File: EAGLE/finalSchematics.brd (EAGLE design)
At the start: 100 x 80 mm, 13 parts, among them IC1 STM32F103RBT, P1 DM3CS-SF, Q1 8MHz 131-220

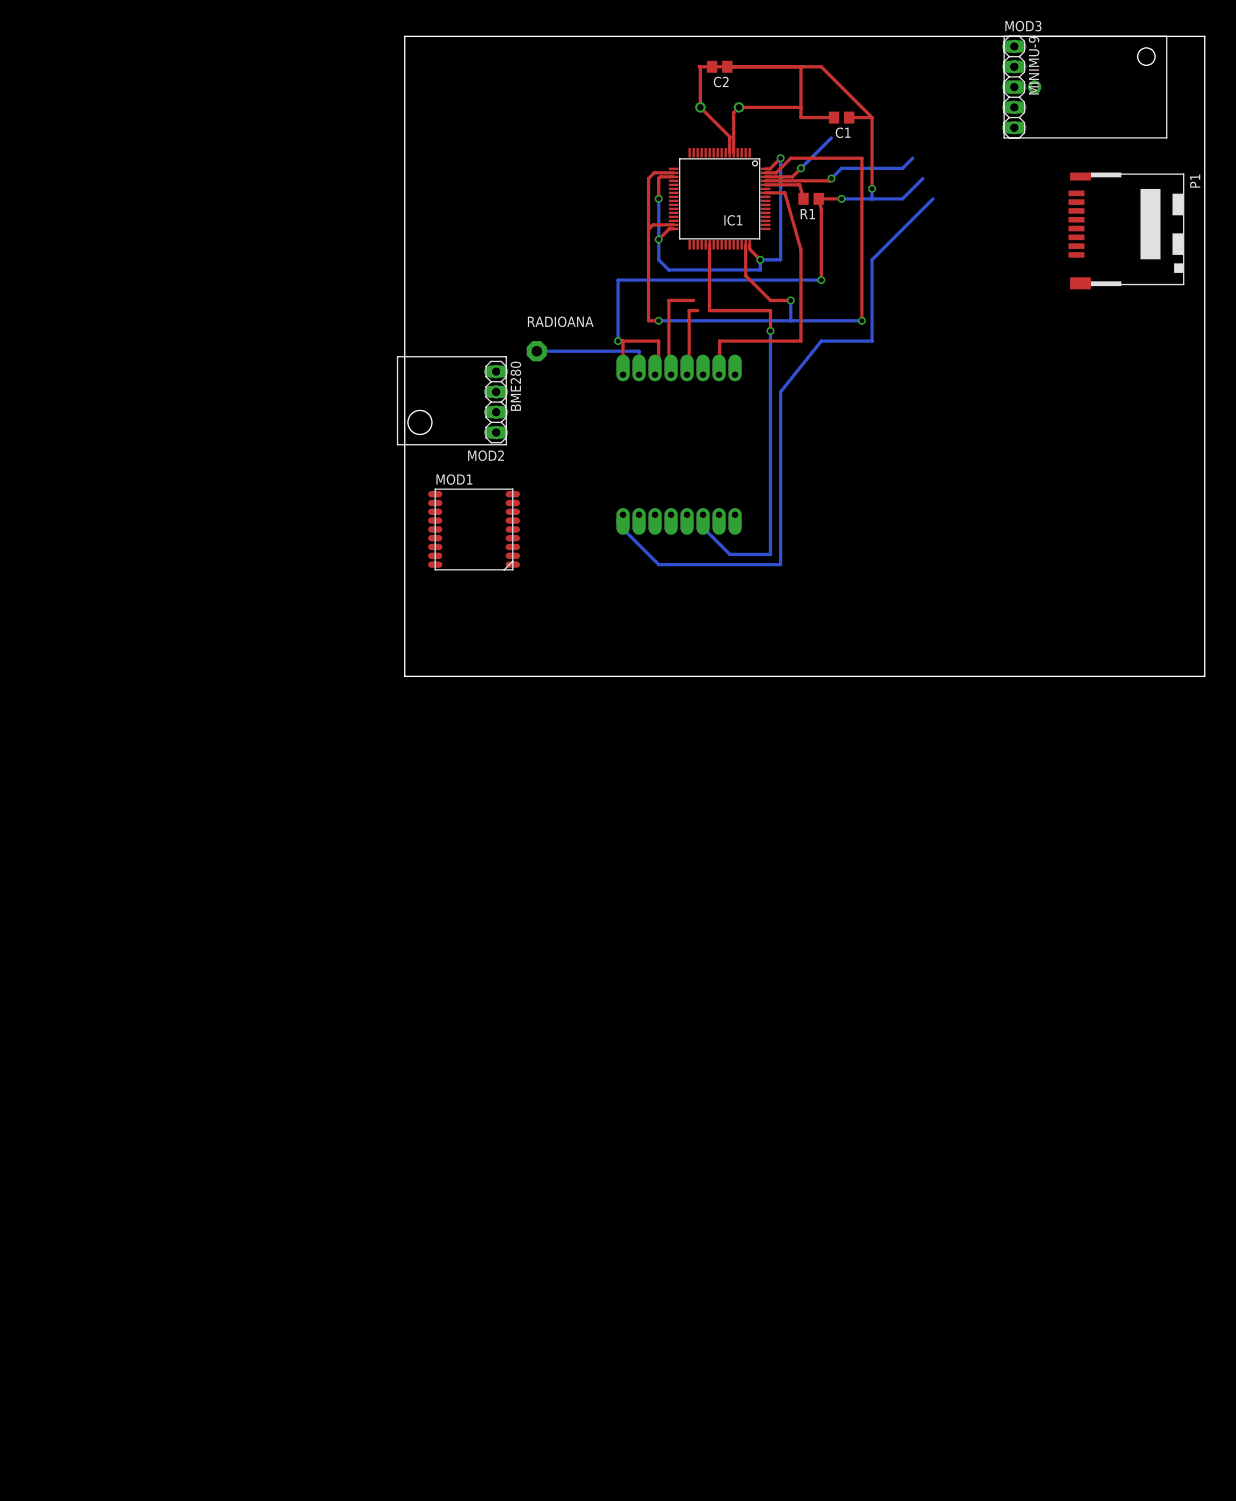
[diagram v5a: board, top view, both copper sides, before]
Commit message: Add SD package, fix powers supply of MCU
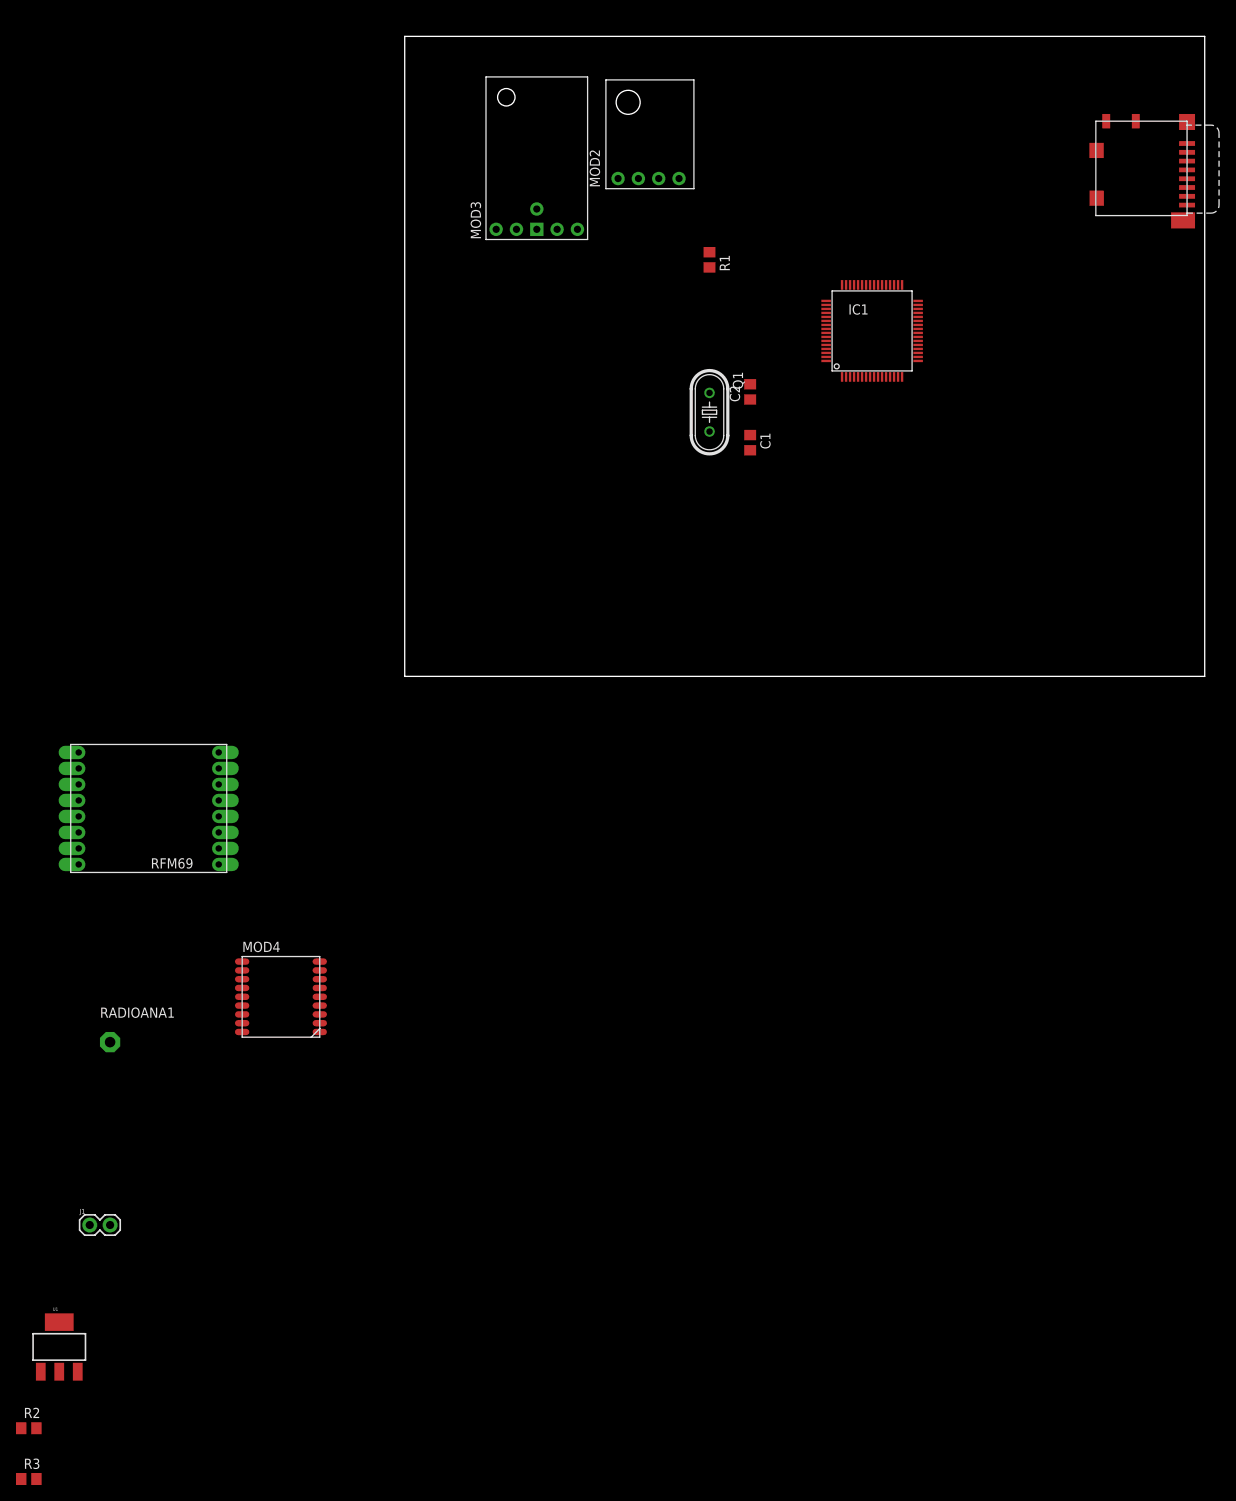
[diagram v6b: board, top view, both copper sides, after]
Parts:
- removed BME280: (no value), pinhead:1X04
- removed MINIMU-9: (no value), pinhead:1X05
- removed MOD1: GPS, components:L70B-GPS
- removed P1: DM3CS-SF, DM3CS-SF:HRS_DM3CS-SF
- removed RADIOANA: (no value), discrete:PAD-01
- removed U$1: RFM69, RFM69mod:20X16BOARD
- added J1: (no value), SparkFun-Connectors:1X02
- added MOD4: GPS, components:L70B-GPS
- added R2, R3: 10k 901-655, rcl:R0805
- added RADIOANA1: (no value), discrete:PAD-01
- added SD1: (no value), components:MOLEX-SD-104031
- added U$2: RFM69, RFM69mod:20X16BOARD
- added U1: LM1117-3.3, SparkFun-IC-Power:SOT223
- IC1: device micro-stm_v3:LQFP64 -> components:LQFP64
- MOD2: value (none) -> BME280
- moved MOD3 62.3 mm to (16.5, 55.9), turned to 90 degrees
- moved C1 42.2 mm to (43.2, 29.2), turned to 270 degrees
- moved C2 40.8 mm to (43.2, 35.6), turned to 90 degrees
- moved Q1 38.1 mm to (38.1, 33.0), flipped to the top, turned to 270 degrees
- moved MOD2 31.4 mm to (35.6, 61.0), turned to 90 degrees
- moved IC1 25.2 mm to (58.4, 43.2), turned to 0 degrees
- moved R1 14.8 mm to (38.1, 52.1), turned to 270 degrees
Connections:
- removed net CS: IC1.43, P1.2
- removed net MISO: IC1.35, P1.7
- removed net MOSI: IC1.36, P1.3
- removed net SCK: IC1.34, P1.5
- removed net VDDA: IC1.13
- removed net VSS: IC1.18, IC1.31, IC1.47, IC1.63
- removed net VSSA: IC1.12
- new net N$5: RADIOANA1.1, U$2.ANA
- net +3V3: now also IC1.13, IC1.19, IC1.32, IC1.48, IC1.64, MOD2.VIN, MOD3.VDD, R2.2, R3.2, SD1.VDD, U$2.3.3V, U1.2, U1.4; no longer BME280.1, MINIMU-9.5, P1.4, U$1.3.3V
- net DIO1_MODEM: now also U$2.DIO1; no longer IC1.38, U$1.DIO1
- net GND: now also IC1.12, IC1.18, IC1.31, IC1.47, IC1.63, J1.2, MOD2.GND, MOD3.GND, MOD4.GND1, MOD4.GND2, MOD4.GND3, SD1.GND@1, SD1.GND@2, SD1.GND@3, SD1.GND@4, SD1.SW1, SD1.SW2, SD1.VSS, U$2.GND@1, U$2.GND@2, U1.1; no longer BME280.2, MINIMU-9.3, MOD1.GND1, MOD1.GND2, MOD1.GND3, P1.6, U$1.GND@1, U$1.GND@2
- net MISO_MODEM: now also U$2.MISO; no longer U$1.MISO
- net MOSI_MODEM: now also U$2.MOSI; no longer U$1.MOSI
- net N$3: now also J1.1, U1.3; no longer RADIOANA.1, U$1.ANA
- net NC: now also U$2.NC; no longer U$1.NC
- net NSS_MODEM: now also U$2.NSS; no longer IC1.58, U$1.NSS
- net RX: now also MOD4.RXD1; no longer MOD1.RXD1
- net SCK_MODEM: now also U$2.SCK; no longer U$1.SCK
- net SCL: now also MOD2.SCL, MOD3.SCL, R3.1; no longer BME280.3, IC1.19, IC1.32, IC1.48, IC1.64, MINIMU-9.1
- net SDA: now also MOD2.SDA, MOD3.SDA, R2.1; no longer BME280.4, MINIMU-9.2
- net TX: now also MOD4.TXD1; no longer MOD1.TXD1
- net VCC: now also MOD4.VCC; no longer MOD1.VCC
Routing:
- net GND: track 105.6 -> 0.00 mm, vias 4 -> 0
- net VSS: track 97.7 -> 0.00 mm, vias 3 -> 0
- net +3V3: track 80.8 -> 0.00 mm
- net SCL: track 68.7 -> 0.00 mm, vias 5 -> 0
- net DIO1_MODEM: track 58.2 -> 0.00 mm, vias 1 -> 0
- net NSS_MODEM: track 35.6 -> 0.00 mm
- net N$1: track 30.2 -> 0.00 mm
- net N$2: track 19.2 -> 0.00 mm
- net N$3: track 15.7 -> 0.00 mm
- net SCK_MODEM: track 12.6 -> 0.00 mm
- net SDA: track 10.2 -> 0.00 mm, vias 1 -> 0
- net MISO_MODEM: track 9.34 -> 0.00 mm
- net BOOT0: track 6.06 -> 0.00 mm

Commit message: Connect modules
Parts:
- moved U$2 64.3 mm to (24.1, 15.2)
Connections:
- removed net DIO1_MODEM: U$2.DIO1
- removed net MISO_MODEM: U$2.MISO
- removed net MOSI_MODEM: U$2.MOSI
- removed net NSS_MODEM: U$2.NSS
- removed net SCK_MODEM: U$2.SCK
- removed net VCC: MOD4.VCC
- new net CS-RAD: IC1.41, U$2.NSS
- new net CS-SD: IC1.20, SD1.CD/DAT3
- new net DIO0: IC1.44, U$2.DIO0
- new net MISO: IC1.22, SD1.DAT0, U$2.MISO
- new net MOSI: IC1.23, SD1.CMD, U$2.MOSI
- new net N$6: MOD4.RF_IN
- new net SCK: IC1.21, SD1.CLK, U$2.SCK
- net +3V3: now also MOD4.VCC
- net RX: now also IC1.42
- net TX: now also IC1.43
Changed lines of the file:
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@@
 <?xml version="1.0" encoding="utf-8"?>
 <!DOCTYPE eagle SYSTEM "eagle.dtd">
-<eagle version="8.1.0">
+<eagle version="8.0.0">
 <drawing>
 <settings>
@@
 <element name="R1" library="rcl" package="R0805" value="10k 901-655" x="38.1" y="52.07" rot="R270"/>
 <element name="SD1" library="components" package="MOLEX-SD-104031" value="" x="97.79" y="63.5" rot="R90"/>
-<element name="U$2" library="RFM69mod" package="20X16BOARD" value="RFM69" x="-31.75" y="-16.51"/>
+<element name="U$2" library="RFM69mod" package="20X16BOARD" value="RFM69" x="24.13" y="15.24"/>
 <element name="RADIOANA1" library="discrete" package="PAD-01" value="" x="-36.83" y="-45.72"/>
 <element name="MOD4" library="components" package="L70B-GPS" value="GPS" x="-20.32" y="-44.45"/>
@@
 <wire x1="29.21" y1="62.23" x2="38.1" y2="53.02" width="0" layer="19" extent="1-1"/>
 <wire x1="16.51" y1="55.88" x2="29.21" y2="62.23" width="0" layer="19" extent="1-1"/>
-<wire x1="-23.25" y1="-19.51" x2="43.18" y2="30.16" width="0" layer="19" extent="1-1"/>
-<wire x1="-23.25" y1="-23.51" x2="-23.25" y2="-19.51" width="0" layer="19" extent="1-1"/>
-<wire x1="-20.32" y1="-35.65" x2="-23.25" y2="-23.51" width="0" layer="19" extent="1-1"/>
+<wire x1="32.63" y1="12.24" x2="43.18" y2="30.16" width="0" layer="19" extent="1-1"/>
+<wire x1="32.63" y1="8.24" x2="32.63" y2="12.24" width="0" layer="19" extent="1-1"/>
+<wire x1="-20.32" y1="-35.65" x2="32.63" y2="8.24" width="0" layer="19" extent="1-1"/>
 <wire x1="-20.32" y1="-37.85" x2="-20.32" y2="-35.65" width="0" layer="19" extent="1-1"/>
 <wire x1="-10.62" y1="-44.45" x2="-20.32" y2="-37.85" width="0" layer="19" extent="1-1"/>
@@
 <signal name="NC">
 <contactref element="U$2" pad="NC"/>
-</signal>
-<signal name="VCC">
-<contactref element="MOD4" pad="VCC"/>
 </signal>
 <signal name="VBAT">
@@
 <contactref element="R2" pad="2"/>
 <contactref element="R3" pad="2"/>
+<contactref element="MOD4" pad="VCC"/>
 <wire x1="64.17" y1="46.93" x2="97.79" y2="63.305" width="0" layer="19" extent="1-1"/>
 <wire x1="64.17" y1="40.43" x2="64.17" y2="46.93" width="0" layer="19" extent="1-1"/>
@@
 <wire x1="26.67" y1="62.23" x2="54.67" y2="48.93" width="0" layer="19" extent="1-1"/>
 <wire x1="21.59" y1="55.88" x2="26.67" y2="62.23" width="0" layer="19" extent="1-1"/>
-<wire x1="-40.75" y1="-23.51" x2="21.59" y2="55.88" width="0" layer="19" extent="1-1"/>
-<wire x1="-43.18" y1="-80.721" x2="-40.75" y2="-23.51" width="0" layer="19" extent="1-1"/>
+<wire x1="-10.62" y1="-36.75" x2="21.59" y2="55.88" width="0" layer="19" extent="1-1"/>
+<wire x1="15.13" y1="8.24" x2="-10.62" y2="-36.75" width="0" layer="19" extent="1-1"/>
+<wire x1="-43.18" y1="-80.721" x2="-10.62" y2="-36.75" width="0" layer="19" extent="1-1"/>
 <wire x1="-43.18" y1="-86.9188" x2="-43.18" y2="-80.721" width="0" layer="19" extent="1-1"/>
 <wire x1="-46.04" y1="-93.98" x2="-43.18" y2="-86.9188" width="0" layer="19" extent="1-1"/>
@@
 <wire x1="38.1" y1="30.607" x2="43.18" y2="28.26" width="0" layer="19" extent="1-1"/>
 </signal>
-<signal name="MOSI_MODEM">
-<contactref element="U$2" pad="MOSI"/>
-</signal>
-<signal name="SCK_MODEM">
-<contactref element="U$2" pad="SCK"/>
-</signal>
-<signal name="DIO1_MODEM">
-<contactref element="U$2" pad="DIO1"/>
-</signal>
-<signal name="NSS_MODEM">
+<signal name="CS-RAD">
 <contactref element="U$2" pad="NSS"/>
-</signal>
-<signal name="MISO_MODEM">
-<contactref element="U$2" pad="MISO"/>
+<contactref element="IC1" pad="41"/>
+<wire x1="32.63" y1="20.24" x2="58.17" y2="48.93" width="0" layer="19" extent="1-1"/>
 </signal>
 <signal name="RX">
 <contactref element="MOD4" pad="RXD1"/>
+<contactref element="IC1" pad="42"/>
+<wire x1="-10.62" y1="-42.25" x2="57.67" y2="48.93" width="0" layer="19" extent="1-1"/>
 </signal>
 <signal name="TX">
 <contactref element="MOD4" pad="TXD1"/>
+<contactref element="IC1" pad="43"/>
+<wire x1="-10.62" y1="-43.35" x2="57.17" y2="48.93" width="0" layer="19" extent="1-1"/>
 </signal>
 <signal name="N$5">
 <contactref element="U$2" pad="ANA"/>
 <contactref element="RADIOANA1" pad="1"/>
-<wire x1="-23.25" y1="-21.51" x2="-36.83" y2="-45.72" width="0" layer="19" extent="1-1"/>
+<wire x1="32.63" y1="10.24" x2="-36.83" y2="-45.72" width="0" layer="19" extent="1-1"/>
 </signal>
 <signal name="N$3">
@@
 <wire x1="-39.37" y1="-68.58" x2="-40.8686" y2="-86.9188" width="0" layer="19" extent="1-1"/>
 </signal>
+<signal name="N$6">
+<contactref element="MOD4" pad="RF_IN"/>
+</signal>
+<signal name="MISO">
+<contactref element="SD1" pad="DAT0"/>
+<contactref element="U$2" pad="MISO"/>
+<contactref element="IC1" pad="22"/>
+<wire x1="64.17" y1="41.93" x2="97.79" y2="60.005" width="0" layer="19" extent="1-1"/>
+<wire x1="32.63" y1="16.24" x2="64.17" y2="41.93" width="0" layer="19" extent="1-1"/>
+</signal>
+<signal name="SCK">
+<contactref element="SD1" pad="CLK"/>
+<contactref element="U$2" pad="SCK"/>
+<contactref element="IC1" pad="21"/>
+<wire x1="64.17" y1="41.43" x2="97.79" y2="62.205" width="0" layer="19" extent="1-1"/>
+<wire x1="32.63" y1="14.24" x2="64.17" y2="41.43" width="0" layer="19" extent="1-1"/>
+</signal>
+<signal name="MOSI">
+<contactref element="SD1" pad="CMD"/>
+<contactref element="U$2" pad="MOSI"/>
+<contactref element="IC1" pad="23"/>
+<wire x1="64.17" y1="42.43" x2="97.79" y2="64.405" width="0" layer="19" extent="1-1"/>
+<wire x1="32.63" y1="18.24" x2="64.17" y2="42.43" width="0" layer="19" extent="1-1"/>
+</signal>
+<signal name="CS-SD">
+<contactref element="SD1" pad="CD/DAT3"/>
+<contactref element="IC1" pad="20"/>
+<wire x1="64.17" y1="40.93" x2="97.79" y2="65.505" width="0" layer="19" extent="1-1"/>
+</signal>
+<signal name="DIO0">
+<contactref element="U$2" pad="DIO0"/>
+<contactref element="IC1" pad="44"/>
+<wire x1="15.13" y1="20.24" x2="56.67" y2="48.93" width="0" layer="19" extent="1-1"/>
+</signal>
 </signals>

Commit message: Final schematic ready to control
Start creating the board itself
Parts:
- removed R1: 10k 901-655, rcl:R0805
- removed RADIOANA1: (no value), discrete:PAD-01
- added 1NF, C10, C11, C3, C6, C7, C8, C9: (no value), rcl:C0805
- added 270OHM, 270OHM1, 270OHM2: (no value), resistor:R0805
- added C4, C5: 47uF, rcl:153CLV-0810
- added D1: 1N4004, diode:DO41-10
- added J2, J3: U.FL, SparkFun-Connectors:U.FL
- added JP1: (no value), pinhead:1X03
- added JP2: (no value), pinhead:1X05
- added LED1, LED2, LED3: (no value), led:CHIP-LED0603
- moved R2 139.3 mm to (54.6, 1.27)
- moved R3 139.3 mm to (54.6, -5.08)
- moved U1 139.3 mm to (58.4, 11.4)
- moved MOD4 71.9 mm to (38.1, -2.54)
- moved U$2 19.4 mm to (17.8, 33.5)
- moved MOD3 18.9 mm to (10.2, 73.7)
- moved MOD2 12.0 mm to (31.8, 72.4)
- moved IC1 2.84 mm to (59.7, 45.7)
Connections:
- removed net BOOT0: IC1.60, R1.2
- new net 1PPS: IC1.3, MOD4.1PPS
- new net N$10: 270OHM.2, IC1.40
- new net N$11: 270OHM.1, LED1.A
- new net N$12: 270OHM1.1, LED2.A
- new net N$13: 270OHM2.1, LED3.A
- new net N$4: D1.A, J1.1
- new net N$7: 270OHM1.2, IC1.38
- new net N$8: 1NF.2, IC1.7
- new net N$9: 270OHM2.2, IC1.39
- new net NRST: 1NF.1, JP2.1
- new net RXDBG: IC1.17, JP1.1
- new net SWCLOCK: IC1.49, JP2.4
- new net SWDIO: IC1.46, JP2.3
- new net SWO: IC1.55, JP2.2
- new net TXDBG: IC1.16, JP1.2
- net +3V3: now also C10.1, C11.1, C3.1, C5.+, C6.1, C7.1, C8.1, C9.1
- net GND: now also C10.2, C11.2, C3.2, C4.-, C5.-, C6.2, C7.2, C8.2, C9.2, J2.P$1, J2.P$2, J3.P$1, J3.P$2, JP1.3, JP2.5, LED1.C, LED2.C, LED3.C; no longer R1.1
- net N$3: now also C4.+, D1.C; no longer J1.1
- net N$5: now also J3.P$3; no longer RADIOANA1.1
- net N$6: now also J2.P$3
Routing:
- net SDA: track 0.00 -> 87.2 mm
- net SCL: track 0.00 -> 82.9 mm, vias 0 -> 1
- net GND: track 0.00 -> 76.1 mm, vias 0 -> 2
- net +3V3: track 0.00 -> 69.5 mm, vias 0 -> 2
